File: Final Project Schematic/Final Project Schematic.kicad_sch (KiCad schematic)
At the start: 43 parts, among them M1 Motor_Servo, Q2 MOSFET-N, Q2 Photo_NPN, Q3 MOSFET-N, Q4 MOSFET-N, SW1 FIRE BUT, SW1 RESET, U1 MCP6294, U1 PIC32MX170F256B, U2 LM339AN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

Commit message: Initial Electrical Schematic
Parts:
- added C4: 0.1 uF, symbol ME218_BaseLib:Cap
- added U2: 74xxx244, symbol ME218_BaseLib:74xxx244
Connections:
- net +5V: now also C4.1, U2.20 (VCC)
- net GNDREF: now also U2.1 (1OE), U2.10 (GND), U2.19 (2OE)
- net at U3.3 (Din): now also U2.14 (1Y2); no longer U1.3 (RA1)
- net at U3.4 (CS): now also U2.16 (1Y1); no longer U1.2 (RA0)
- net at U3.5 (Clk): now also U2.18 (1Y0); no longer U1.25 (RB14)
- new net: U1.25 (RB14), U2.2 (1A0)
- new net: U1.3 (RA1), U2.4 (1A1)
- new net: U1.2 (RA0), U2.6 (1A2)
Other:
- note added: "CLK"
- note added: "SDO"
- note added: "~{SS}"
- moved on the sheet: C1, C2, C3, U1, U3

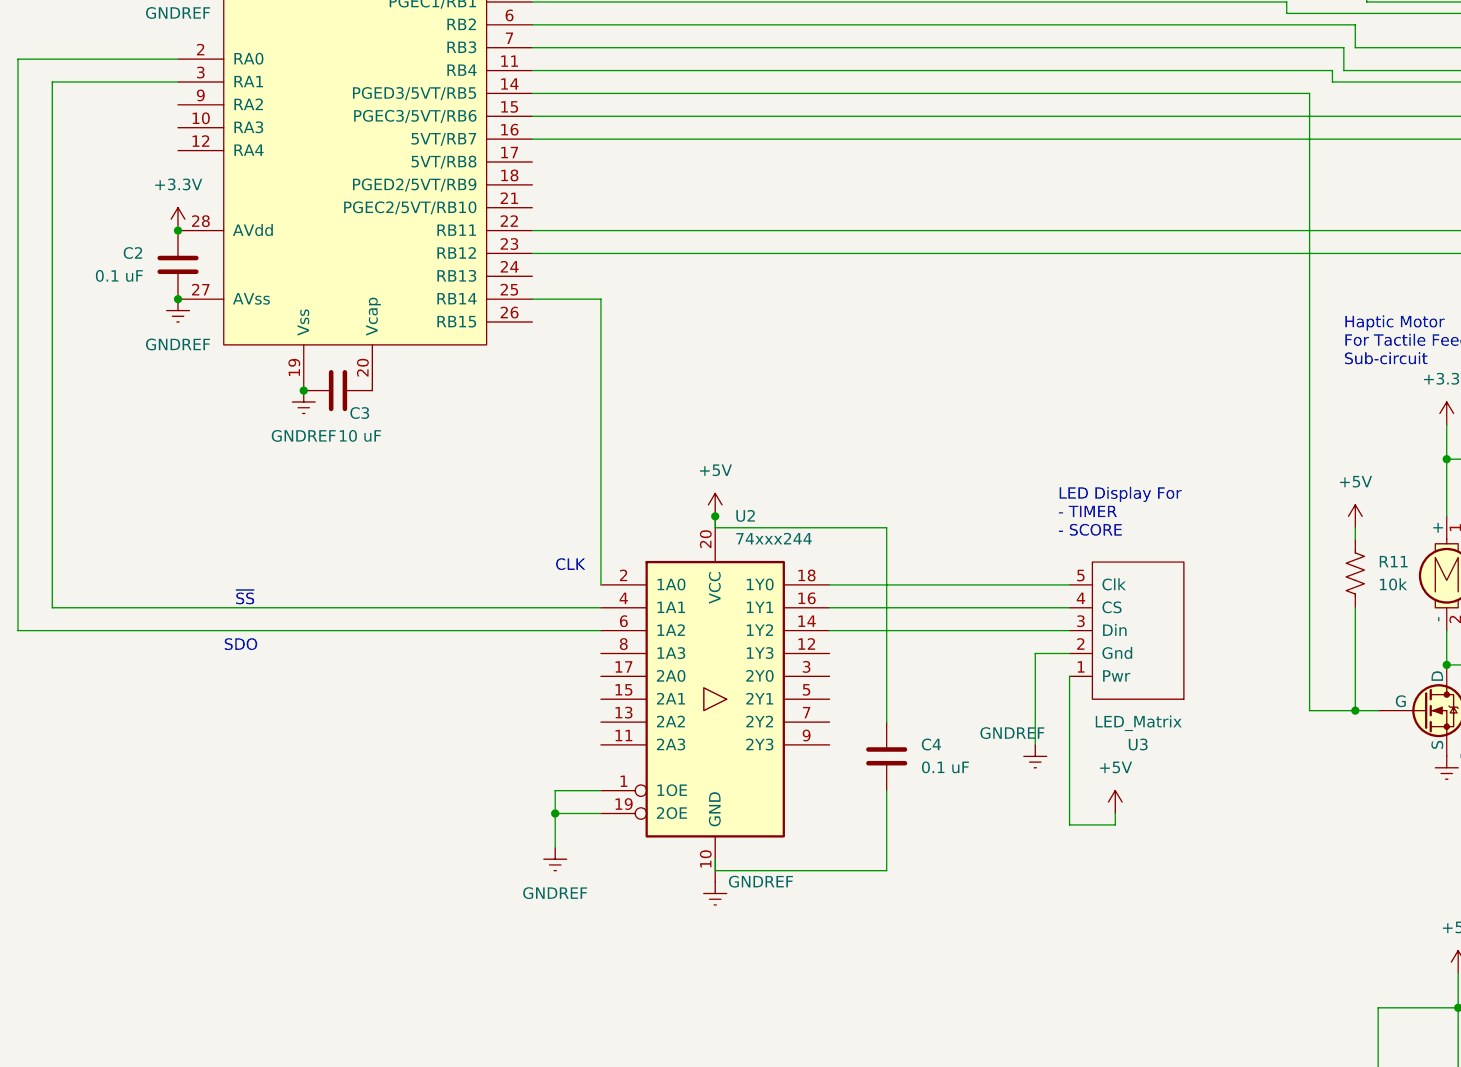
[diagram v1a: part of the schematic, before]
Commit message: Added LED for the Turret to the Electrical Schematic
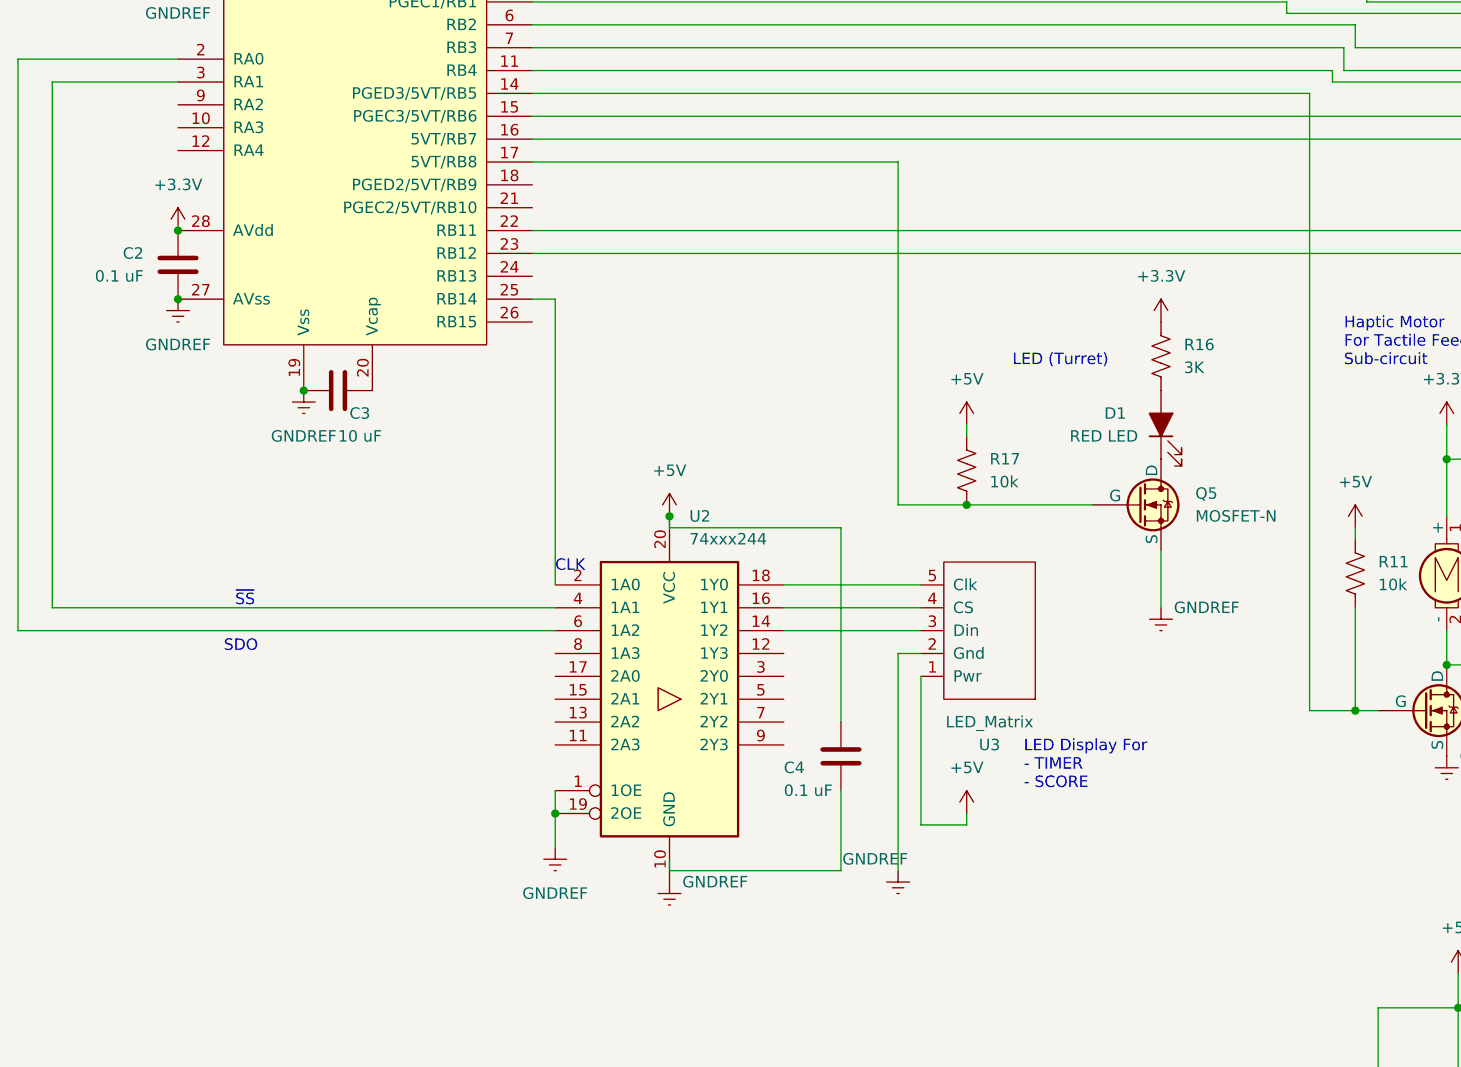
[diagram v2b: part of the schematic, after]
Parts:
- added D1: RED LED, symbol ME218_BaseLib:LED
- added Q5: MOSFET-N, symbol ME218_BaseLib:MOSFET-N
- added R16: 3K, symbol ME218_BaseLib:Res1
- added R17: 10k, symbol ME218_BaseLib:Res1
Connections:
- net +3.3V: now also R16.1
- net +5V: now also R17.1
- net GNDREF: now also Q5.3 (S)
- net at U1.17 (5VT/RB8): now also Q5.2 (G), R17.2
- new net: D1.2 (A), R16.2
- new net: D1.1 (K), Q5.1 (D)
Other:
- note added: "LED (Turret)"
- moved on the sheet: C4, U2, U3
